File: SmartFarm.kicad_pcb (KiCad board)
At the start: 2 copper layers, 80 x 80 mm, 39 parts, among them J1 Conn_01x20_Pin, J10 Conn_01x06_Socket, J11 Conn_01x06_Socket, J12 Conn_01x01_Pin, J13 Conn_01x01_Pin, J14 Conn_01x01_Pin, J15 Conn_01x01_Pin, J16 Screw_Terminal_01x02, J2 Conn_01x20_Pin, J4 Conn_01x04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

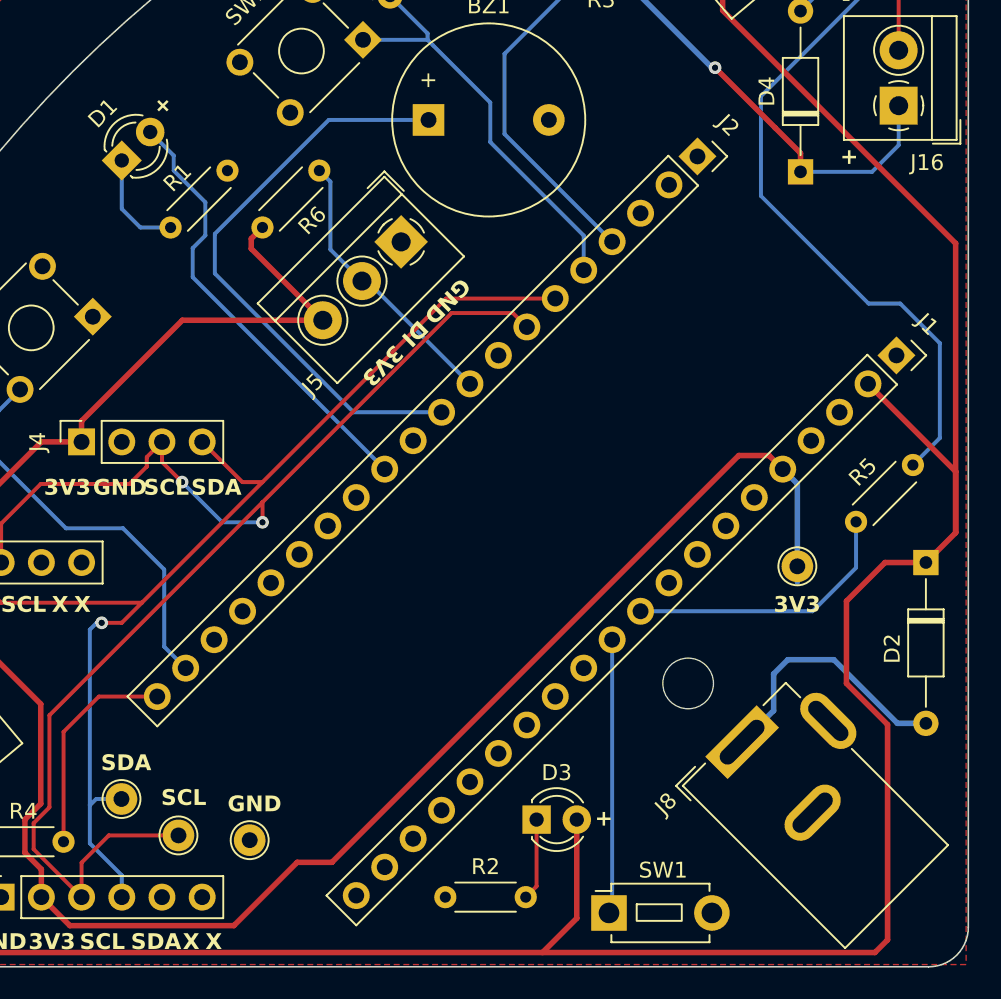
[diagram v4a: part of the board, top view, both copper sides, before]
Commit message: add pico w board
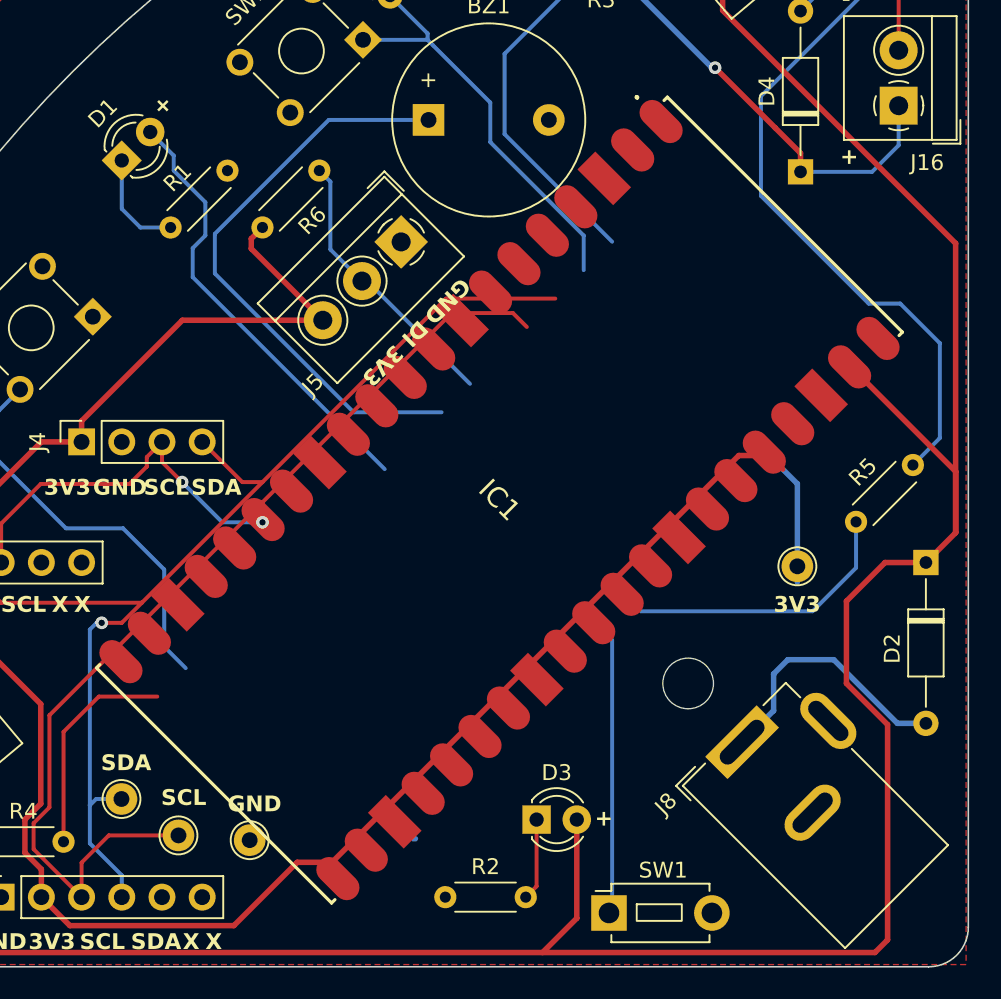
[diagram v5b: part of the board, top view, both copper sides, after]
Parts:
- removed J1, J2: Conn_01x20_Pin, Connector_PinSocket_2.54mm:PinSocket_1x20_P2.54mm_Vertical
- added IC1: RASPBERRY_PI_PICO_W, PICO_W:RASPBERRYPIPICOW, F.Cu at (120.4, 120.5)
- C3, C4: value 1000uF/10V -> 1000uF/6.3V

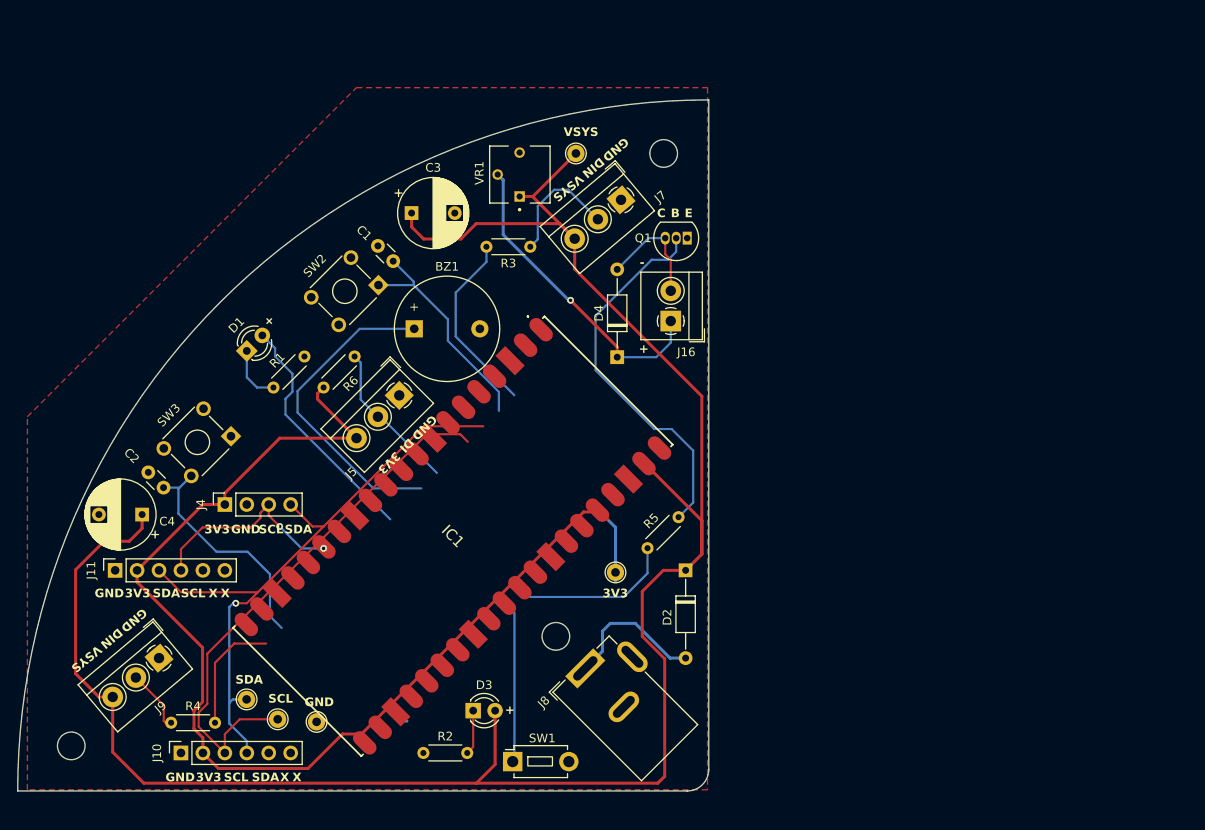
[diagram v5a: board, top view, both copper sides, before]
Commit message: add smd library parts
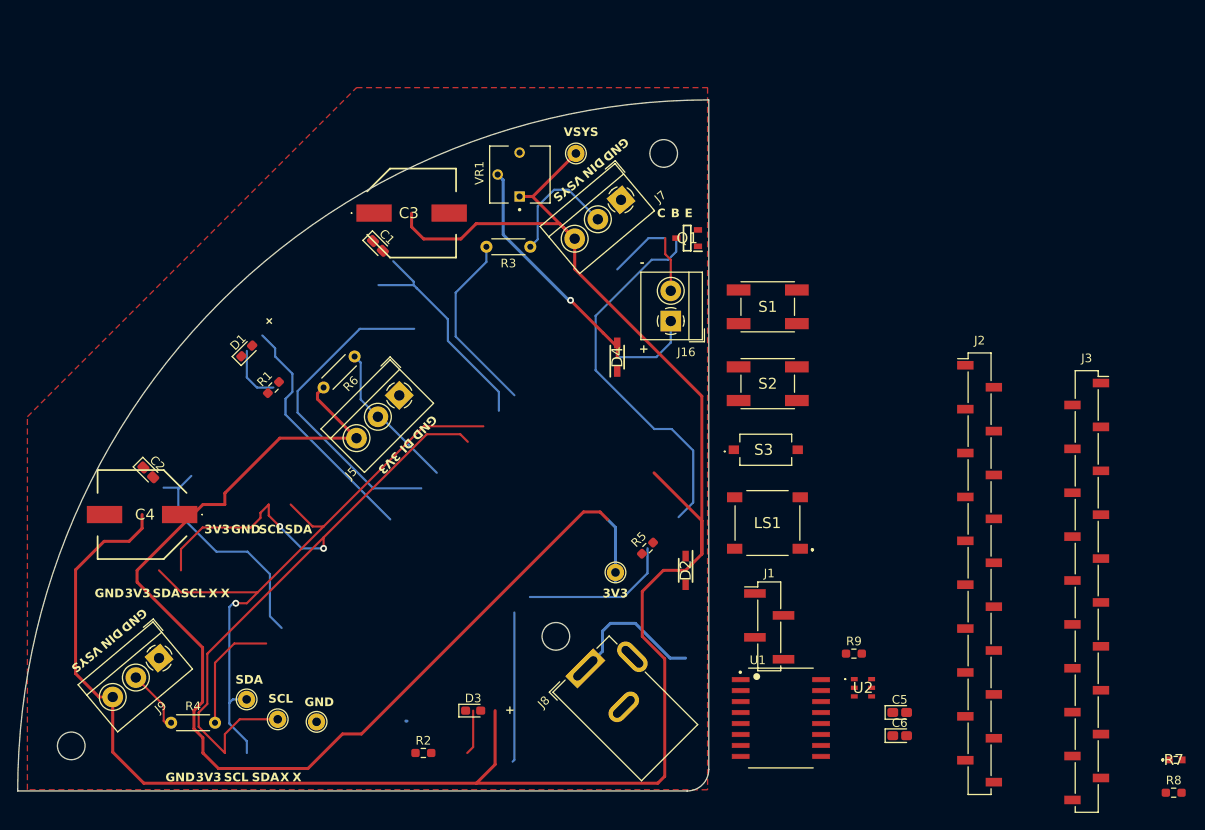
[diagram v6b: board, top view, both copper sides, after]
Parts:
- removed BZ1: Buzzer, Buzzer_Beeper:Buzzer_12x9.5RM7.6
- removed IC1: RASPBERRY_PI_PICO_W, PICO_W:RASPBERRYPIPICOW
- removed J10, J11: Conn_01x06_Socket, Connector_PinSocket_2.54mm:PinSocket_1x06_P2.54mm_Vertical
- removed J4: Conn_01x04, Connector_PinSocket_2.54mm:PinSocket_1x04_P2.54mm_Vertical
- removed SW1: SW_DIP_x01, Button_Switch_THT:SW_PUSH_1P1T_6x3.5mm_H4.3_APEM_MJTP1243
- removed SW2, SW3: SW_MEC_5E, Button_Switch_THT:SW_TH_Tactile_Omron_B3F-10xx
- added C5: 10uF/10V(10%), Capacitor_Tantalum_SMD:CP_EIA-1608-10_AVX-L_Pad1.25x1.05mm_HandSolder, F.Cu at (172.1, 140.9)
- added C6: 0.1uF/10V(10%), Capacitor_Tantalum_SMD:CP_EIA-1608-10_AVX-L_Pad1.25x1.05mm_HandSolder, F.Cu at (172.1, 143.6)
- added J1: Conn_01x04_Socket, Connector_PinHeader_2.54mm:PinHeader_1x04_P2.54mm_Vertical_SMD_Pin1Left, F.Cu at (157.0, 130.9)
- added J2: Conn_01x20_Socket, Connector_PinSocket_2.54mm:PinSocket_1x20_P2.54mm_Vertical_SMD_Pin1Left, F.Cu at (181.3, 124.8)
- added J3: Conn_01x20_Socket, Connector_PinSocket_2.54mm:PinSocket_1x20_P2.54mm_Vertical_SMD_Pin1Right, F.Cu at (193.8, 126.9)
- added LS1: MLT-7525, LIB_MLT-7525:MLT7525, F.Cu at (156.8, 119.0)
- added R7: ALS-PT19-315C_L177_TR8, ALS-PT19-315C:ALSPT19315CL177TR8, F.Cu at (204.1, 146.4)
- added R8: 10K(5%), Resistor_SMD:R_0603_1608Metric_Pad0.98x0.95mm_HandSolder, F.Cu at (203.8, 150.2)
- added R9: 220, Resistor_SMD:R_0603_1608Metric_Pad0.98x0.95mm_HandSolder, F.Cu at (166.8, 134.1)
- added S1: SKHUAKE010, SKHUAKE010:SKHUAKE010, F.Cu at (156.8, 94.0)
- added S2: SKHUAKE010, SKHUAKE010:SKHUAKE010, F.Cu at (156.8, 102.8)
- added S3: TS-1101-C-W, TS-1101-C-W:TS1101CW, F.Cu at (156.6, 110.5)
- added U1: DS3231SN, DS3231SN:SOIC127P1032X265-16N, F.Cu at (158.3, 141.6)
- added U2: AHT20, AHT20:AHT20, F.Cu at (167.8, 138.1)
- C1, C2: footprint Capacitor_THT:C_Disc_D3.0mm_W1.6mm_P2.50mm -> Capacitor_Tantalum_SMD:CP_EIA-1608-08_AVX-J_Pad1.25x1.05mm_HandSolder
- C3, C4: footprint Capacitor_THT:CP_Radial_D8.0mm_P5.00mm -> EEEHAA102UAP:EEE0JA152UAP
- D1, D3: footprint LED_THT:LED_D3.0mm -> LED_SMD:LED_0603_1608Metric_Pad1.05x0.95mm_HandSolder
- D2, D4: footprint Diode_THT:D_DO-35_SOD27_P10.16mm_Horizontal -> 1N5711W-7-F:SOD3716X115N
- Q1: footprint Package_TO_SOT_THT:TO-92_Inline -> 2N3904S-RTK:2N3904SRTKPS
- R1, R2, R5: footprint Resistor_THT:R_Axial_DIN0204_L3.6mm_D1.6mm_P5.08mm_Horizontal -> Resistor_SMD:R_0603_1608Metric_Pad0.98x0.95mm_HandSolder
